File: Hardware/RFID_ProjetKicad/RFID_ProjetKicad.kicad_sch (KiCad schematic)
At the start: 25 parts, among them J1 TB0011-350-04GR, J2 TB0011-350-04GR, U1 XIAO-ESP32-C6-DIP, U2 CEG006900, U3 MAX3485CSA_T

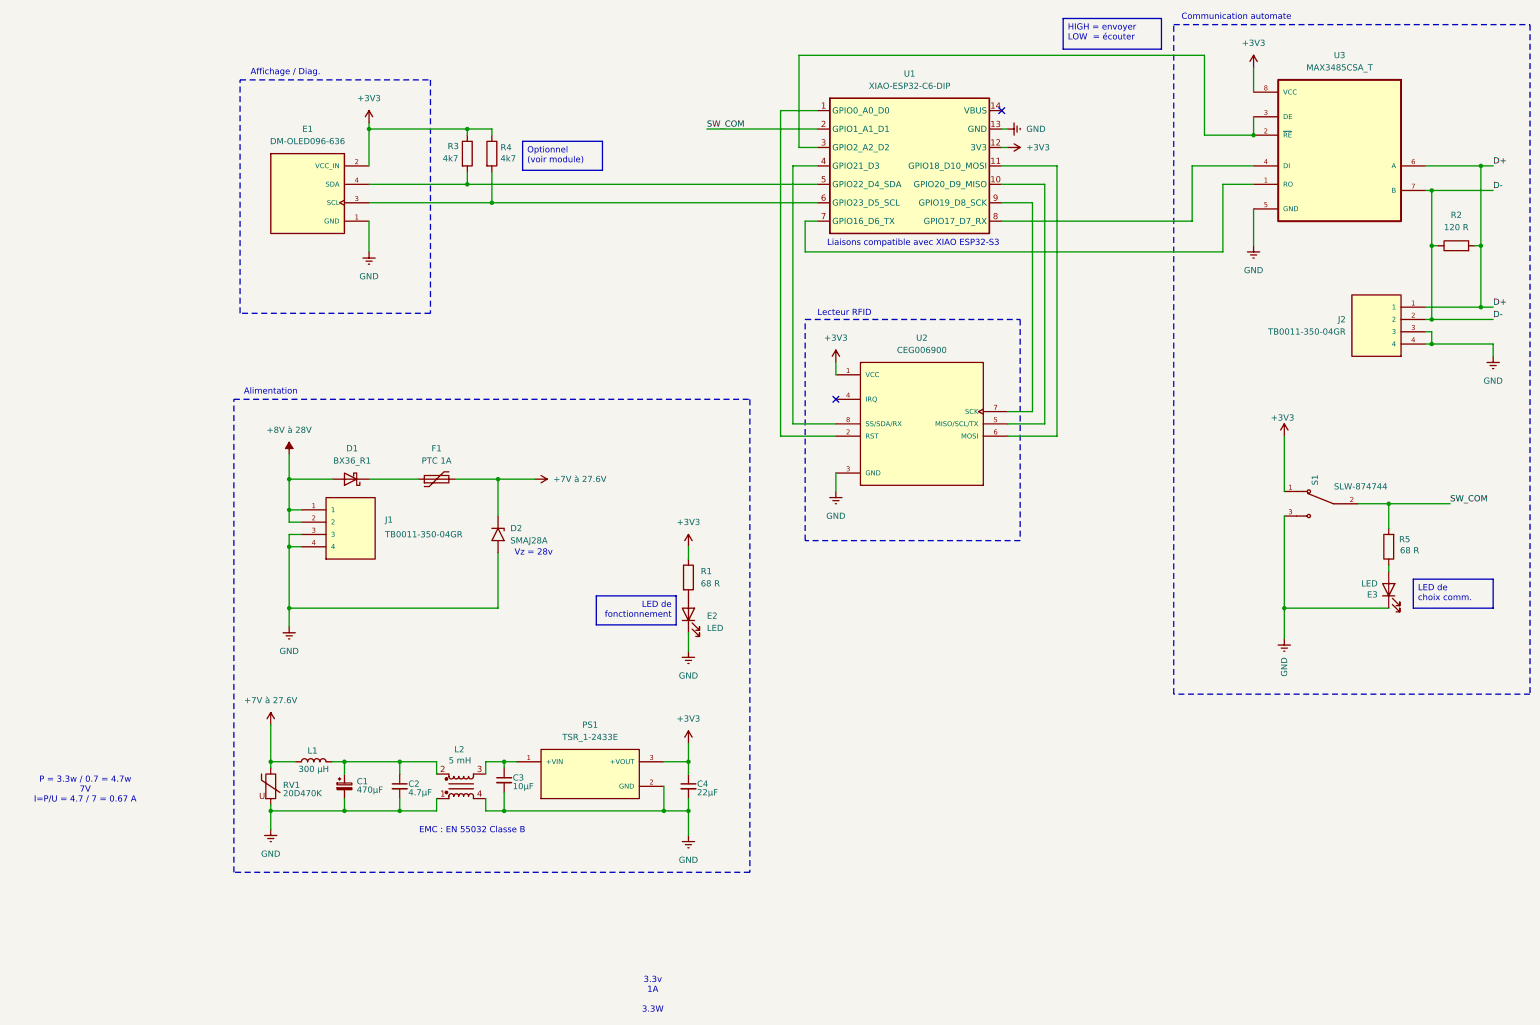
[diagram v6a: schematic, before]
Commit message: Ajout de la documentation sur l'implémentation PCB + Modification PCB et logos
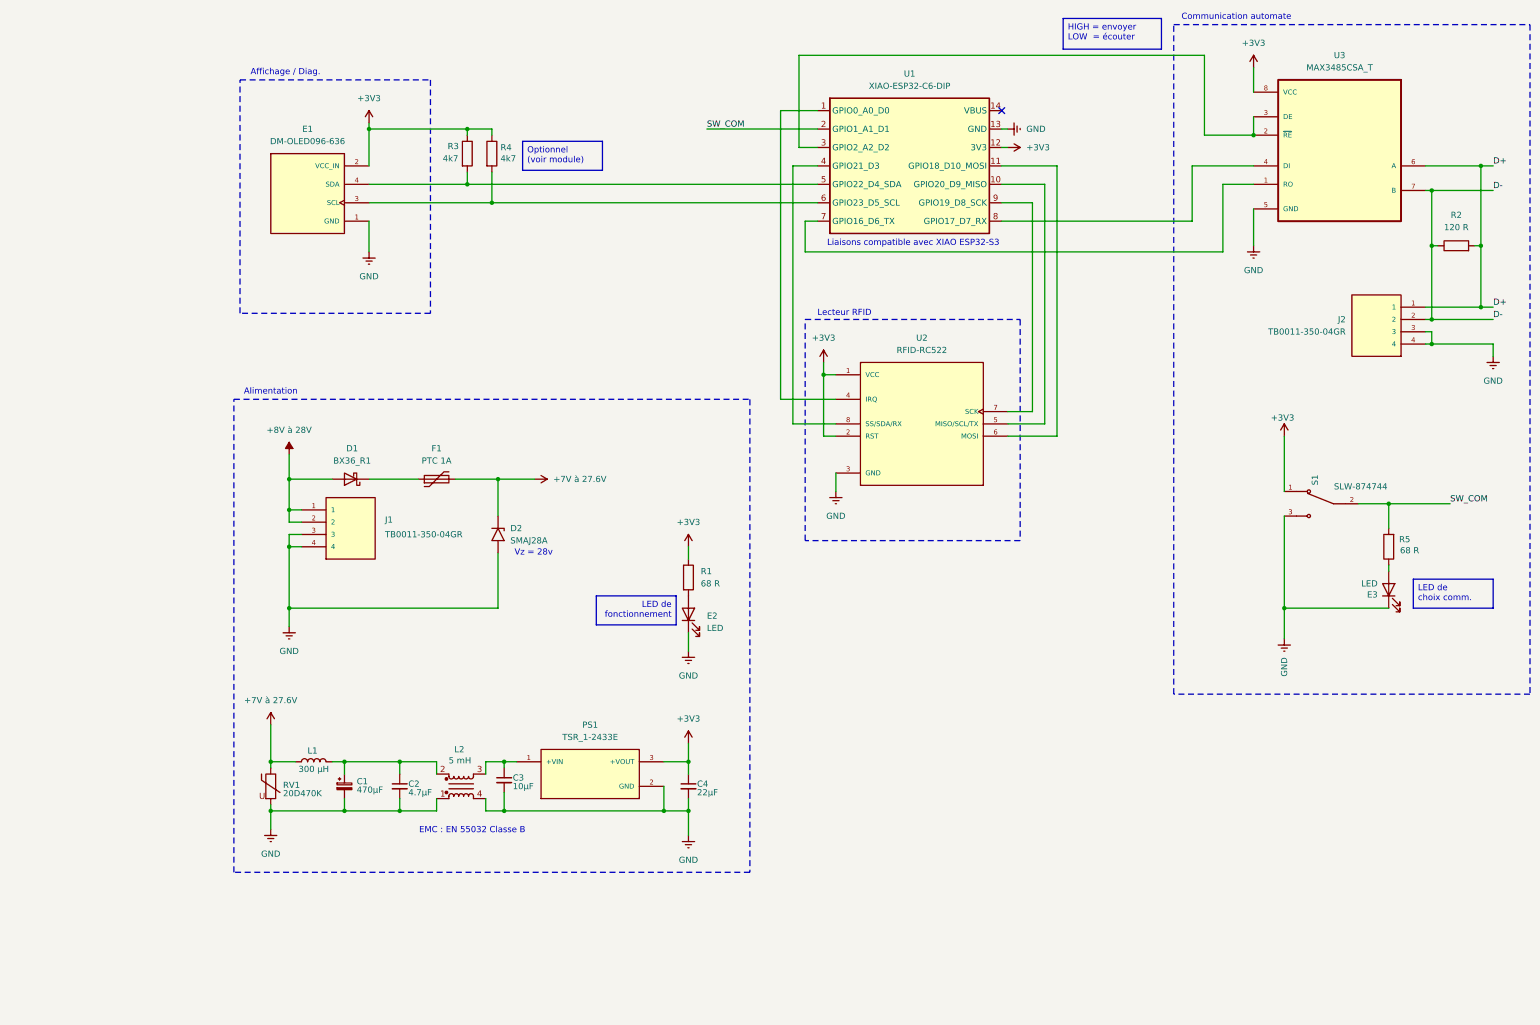
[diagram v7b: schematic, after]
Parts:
- U2: value CEG006900 -> RFID-RC522
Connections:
- net +3V3: now also U2.2 (RST)
- net at U1.1 (GPIO0_A0_D0): now also U2.4 (IRQ); no longer U2.2 (RST)
- no-connect marks 2 -> 1
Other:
- note removed: "3.3v 1A 3.3W"
- note removed: "P = 3.3w / 0.7 = 4.7w 7V I=P/U = 4.7 / 7 = 0.67 A"
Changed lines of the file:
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@@
 		)
 	)
-	(text "P = 3.3w / 0.7 = 4.7w\n7V\nI=P/U = 4.7 / 7 = 0.67 A\n"
-		(exclude_from_sim no)
-		(at -15.494 177.292 0)
-		(effects
-			(font
-				(size 1.27 1.27)
-			)
-		)
-	)
 	(text "Lecteur RFID"
 		(exclude_from_sim no)
@@
 		)
 	)
-	(text "3.3v\n1A\n\n3.3W"
-		(exclude_from_sim no)
-		(at 101.854 219.71 0)
-		(effects
-			(font
-				(size 1.27 1.27)
-			)
-		)
-	)
 	(text "Affichage / Diag."
 		(exclude_from_sim no)
@@
 	)
 	(junction
+		(at 137.16 91.44)
+		(diameter 0)
+		(color 0 0 0 0)
+	)
+	(junction
 		(at 26.67 127)
 		(diameter 0)
@@
 		(at 173.99 36.83)
 	)
-	(no_connect
-		(at 139.7 96.52)
-	)
 	(wire
 		(pts
@@
 	(wire
 		(pts
+			(xy 137.16 91.44) (xy 139.7 91.44)
+		)
+		(stroke
+			(width 0)
+			(type default)
+		)
+	)
+	(wire
+		(pts
 			(xy 68.58 40.64) (xy 68.58 41.91)
 		)
@@
 	(wire
 		(pts
-			(xy 262.89 80.01) (xy 261.62 80.01)
+			(xy 128.27 96.52) (xy 139.7 96.52)
 		)
 		(stroke
@@
 	(wire
 		(pts
-			(xy 139.7 104.14) (xy 128.27 104.14)
+			(xy 262.89 80.01) (xy 261.62 80.01)
 		)
 		(stroke
@@
 	(wire
 		(pts
-			(xy 262.89 53.34) (xy 275.59 53.34)
+			(xy 128.27 36.83) (xy 128.27 96.52)
 		)
 		(stroke
@@
 	(wire
 		(pts
-			(xy 261.62 82.55) (xy 262.89 82.55)
+			(xy 262.89 53.34) (xy 275.59 53.34)
 		)
 		(stroke
@@
 	(wire
 		(pts
-			(xy 67.31 181.61) (xy 71.12 181.61)
+			(xy 261.62 82.55) (xy 262.89 82.55)
 		)
 		(stroke
@@
 	(wire
 		(pts
-			(xy 132.08 25.4) (xy 132.08 44.45)
+			(xy 67.31 181.61) (xy 71.12 181.61)
 		)
 		(stroke
@@
 	(wire
 		(pts
-			(xy 130.81 48.26) (xy 135.89 48.26)
+			(xy 132.08 25.4) (xy 132.08 44.45)
 		)
 		(stroke
@@
 	(wire
 		(pts
-			(xy 43.18 113.03) (xy 53.34 113.03)
+			(xy 130.81 48.26) (xy 135.89 48.26)
 		)
 		(stroke
@@
 	(wire
 		(pts
-			(xy 38.1 171.45) (xy 49.53 171.45)
+			(xy 43.18 113.03) (xy 53.34 113.03)
 		)
 		(stroke
@@
 	(wire
 		(pts
-			(xy 128.27 36.83) (xy 135.89 36.83)
+			(xy 38.1 171.45) (xy 49.53 171.45)
 		)
 		(stroke
@@
 	(wire
 		(pts
-			(xy 232.41 139.7) (xy 232.41 146.05)
+			(xy 135.89 36.83) (xy 128.27 36.83)
 		)
 		(stroke
@@
 	(wire
 		(pts
-			(xy 173.99 40.64) (xy 175.26 40.64)
+			(xy 232.41 139.7) (xy 232.41 146.05)
 		)
 		(stroke
@@
 	(wire
 		(pts
-			(xy 22.86 163.83) (xy 22.86 171.45)
+			(xy 173.99 40.64) (xy 175.26 40.64)
 		)
 		(stroke
@@
 	(wire
 		(pts
-			(xy 128.27 36.83) (xy 128.27 104.14)
+			(xy 22.86 163.83) (xy 22.86 171.45)
 		)
 		(stroke
@@
 	(wire
 		(pts
-			(xy 139.7 88.9) (xy 139.7 91.44)
+			(xy 137.16 88.9) (xy 137.16 91.44)
 		)
 		(stroke
@@
 	(wire
 		(pts
+			(xy 137.16 104.14) (xy 137.16 91.44)
+		)
+		(stroke
+			(width 0)
+			(type default)
+		)
+	)
+	(wire
+		(pts
 			(xy 26.67 139.7) (xy 26.67 143.51)
 		)
@@
 	(wire
 		(pts
+			(xy 139.7 104.14) (xy 137.16 104.14)
+		)
+		(stroke
+			(width 0)
+			(type default)
+		)
+	)
+	(wire
+		(pts
 			(xy 29.21 127) (xy 26.67 127)
 		)
@@
 	(symbol
 		(lib_id "power:+3V3")
-		(at 139.7 88.9 0)
+		(at 137.16 88.9 0)
 		(unit 1)
 		(body_style 1)
@@
 		(fields_autoplaced yes)
 		(property "Reference" "#PWR010"
-			(at 139.7 92.71 0)
+			(at 137.16 92.71 0)
 			(hide yes)
 			(show_name no)
@@
 		)
 		(property "Value" "+3V3"
-			(at 139.7 83.82 0)
+			(at 137.16 83.82 0)
 			(show_name no)
 			(do_not_autoplace no)
@@
 		)
 		(property "Footprint" ""
-			(at 139.7 88.9 0)
+			(at 137.16 88.9 0)
 			(hide yes)
 			(show_name no)
@@
 		)
 		(property "Datasheet" ""
-			(at 139.7 88.9 0)
+			(at 137.16 88.9 0)
 			(hide yes)
 			(show_name no)
@@
 		)
 		(property "Description" "Power symbol creates a global label with name \"+3V3\""
-			(at 139.7 88.9 0)
+			(at 137.16 88.9 0)
 			(hide yes)
 			(show_name no)
@@
 			)
 		)
-		(property "Value" "CEG006900"
+		(property "Value" "RFID-RC522"
 			(at 157.48 86.36 0)
 			(show_name no)
